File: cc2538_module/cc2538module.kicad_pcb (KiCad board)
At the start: 2 copper layers, 49 parts, among them CON1 USB-MICRO-B, J2 XBEE, P1 CONN_2, SW1 JS102011SCQN, U1 TPS769XX, U2 TPS6217X, U3 CC2538, X1 32MHZ, X2 32.768KHz, j9 JTAG

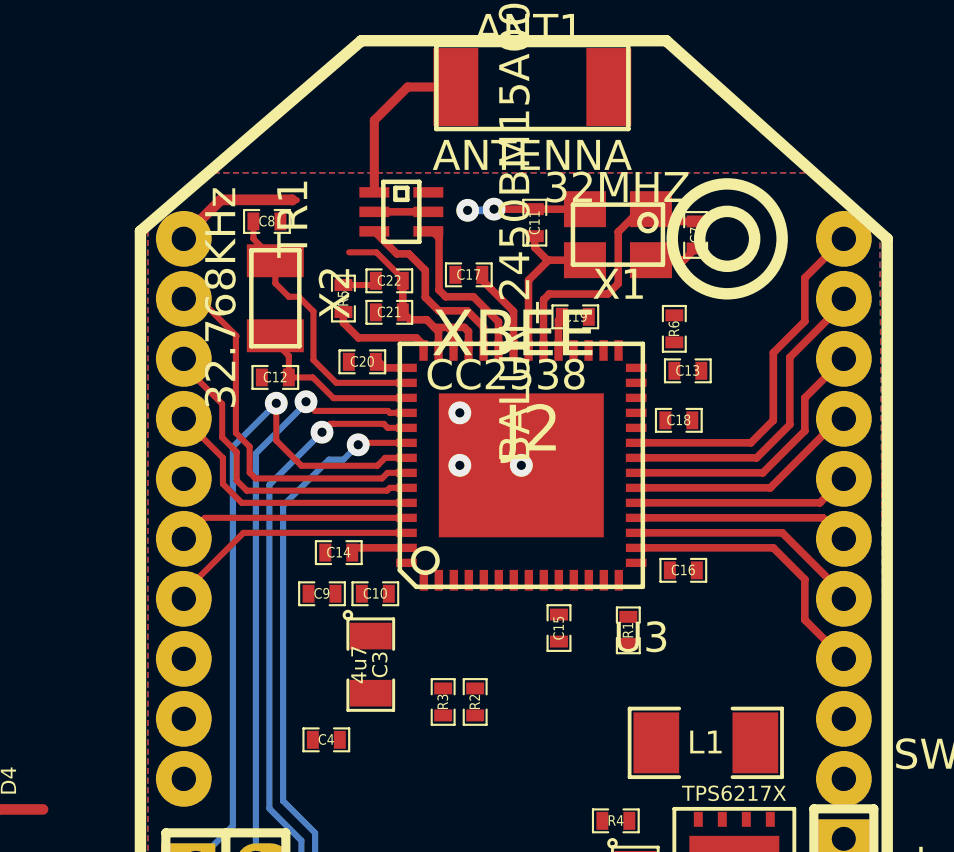
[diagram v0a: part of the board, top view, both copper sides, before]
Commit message: fixed some more routing to the pcb
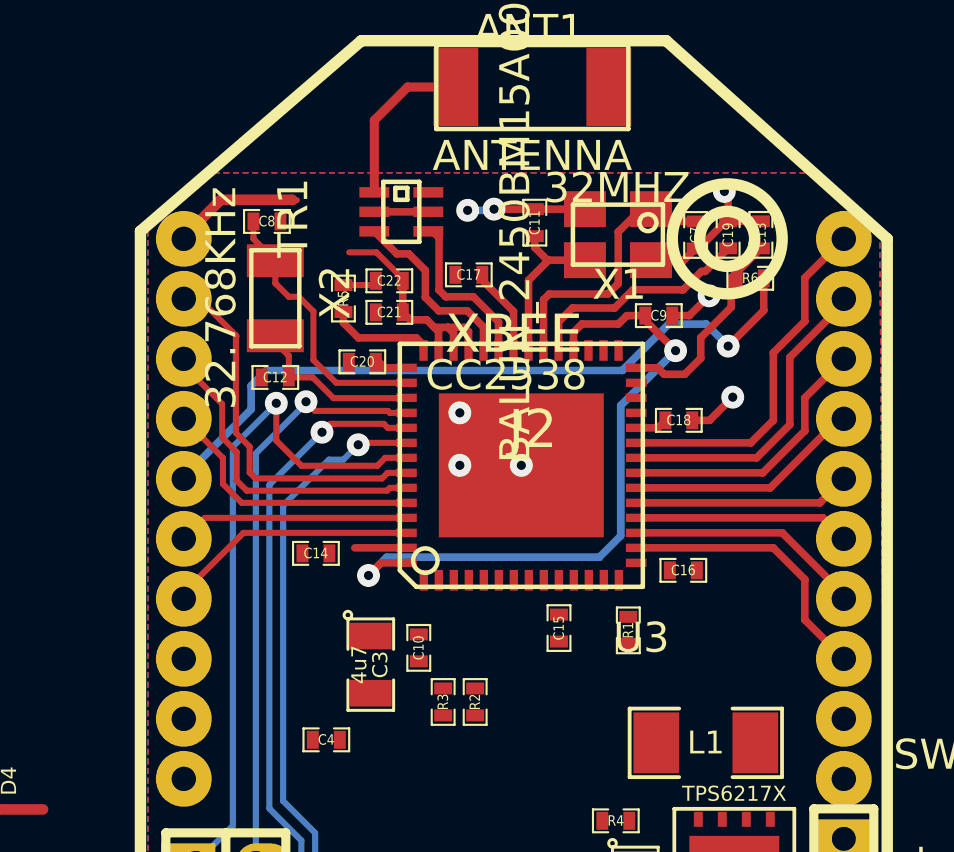
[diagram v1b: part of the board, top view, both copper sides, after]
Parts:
- moved C9 14.6 mm to (59.2, 32.4), turned to 0 degrees
- moved C19 5.78 mm to (61.5, 29.7), turned to 90 degrees
- moved C13 5.15 mm to (62.6, 29.7), turned to 90 degrees
- moved R6 3.04 mm to (62.3, 31.1), turned to 0 degrees
- moved C10 2.31 mm to (51.2, 43.4), turned to 270 degrees
- moved C14 0.76 mm to (47.8, 40.3)
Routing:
- net NRST: track 0.00 -> 23.8 mm, vias 0 -> 1
- net N-0000038: track 0.00 -> 22.1 mm, vias 0 -> 2
- net VDD: track 19.4 -> 26.9 mm
- net N-0000037: track 0.00 -> 7.33 mm
- net GND: track 31.2 -> 38.0 mm, vias 5 -> 8

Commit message: Finished top half of the PCB
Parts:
- moved C18 1.44 mm to (61.3, 35.9)
- moved R6 1.08 mm to (63.2, 31.6), turned to 270 degrees
- moved X2 0.42 mm to (46.1, 31.6)
- moved C8 0.40 mm to (45.8, 29.1), turned to 180 degrees
- moved R5 0.27 mm to (48.8, 31.5)
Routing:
- net VDD: track 26.9 -> 77.1 mm, vias 0 -> 6
- net GND: track 38.0 -> 61.9 mm, vias 8 -> 30
- net NRST: track 23.8 -> 23.2 mm
- net N-0000037: track 7.33 -> 7.91 mm
- net PB5: track 12.4 -> 12.1 mm, vias 0 -> 1

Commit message: Finisched layouting board
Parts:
- moved C5 19.6 mm to (46.4, 40.2)
- moved R9 18.6 mm to (53.7, 47.2), turned to 90 degrees
- moved R10 17.8 mm to (54.0, 45.5), turned to 180 degrees
- moved U1 17.4 mm to (49.2, 50.2), turned to 270 degrees
- moved R8 16.3 mm to (50.4, 44.9), turned to 180 degrees
- moved D2 15.9 mm to (49.9, 47.0)
- moved D3 15.9 mm to (51.2, 47.0)
- moved D4 15.9 mm to (52.5, 47.0)
- moved D1 15.9 mm to (48.5, 47.0)
- moved C2 15.6 mm to (45.8, 48.5), turned to 180 degrees
- moved R7 14.5 mm to (47.4, 45.1)
- moved SW1 12.5 mm to (61.9, 54.1), turned to 270 degrees
- moved R1 9.50 mm to (54.5, 51.6), turned to 180 degrees
- moved C4 6.90 mm to (45.4, 40.2), turned to 90 degrees
- moved R2 5.91 mm to (51.7, 51.0)
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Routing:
- net GND: track 61.9 -> 128.0 mm, vias 30 -> 37
- net VDD: track 77.1 -> 136.0 mm, vias 6 -> 10
- net VDD_USB: track 0.00 -> 26.1 mm, vias 0 -> 4
- net VDD_BCK: track 0.00 -> 21.5 mm
- net USB_N: track 0.00 -> 21.4 mm, vias 0 -> 2
- net NRST: track 23.2 -> 43.5 mm, vias 1 -> 2
- net PC0: track 0.00 -> 17.5 mm, vias 0 -> 2
- net USB_P: track 0.00 -> 17.2 mm, vias 0 -> 2
- net PC7: track 0.00 -> 14.0 mm
- net PC2: track 0.00 -> 13.7 mm
- net PB0: track 0.00 -> 12.6 mm
- net PC1: track 0.00 -> 11.6 mm
- net PC6: track 0.00 -> 9.81 mm
- net VIN: track 0.00 -> 9.34 mm
- net PC4: track 0.00 -> 8.40 mm
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
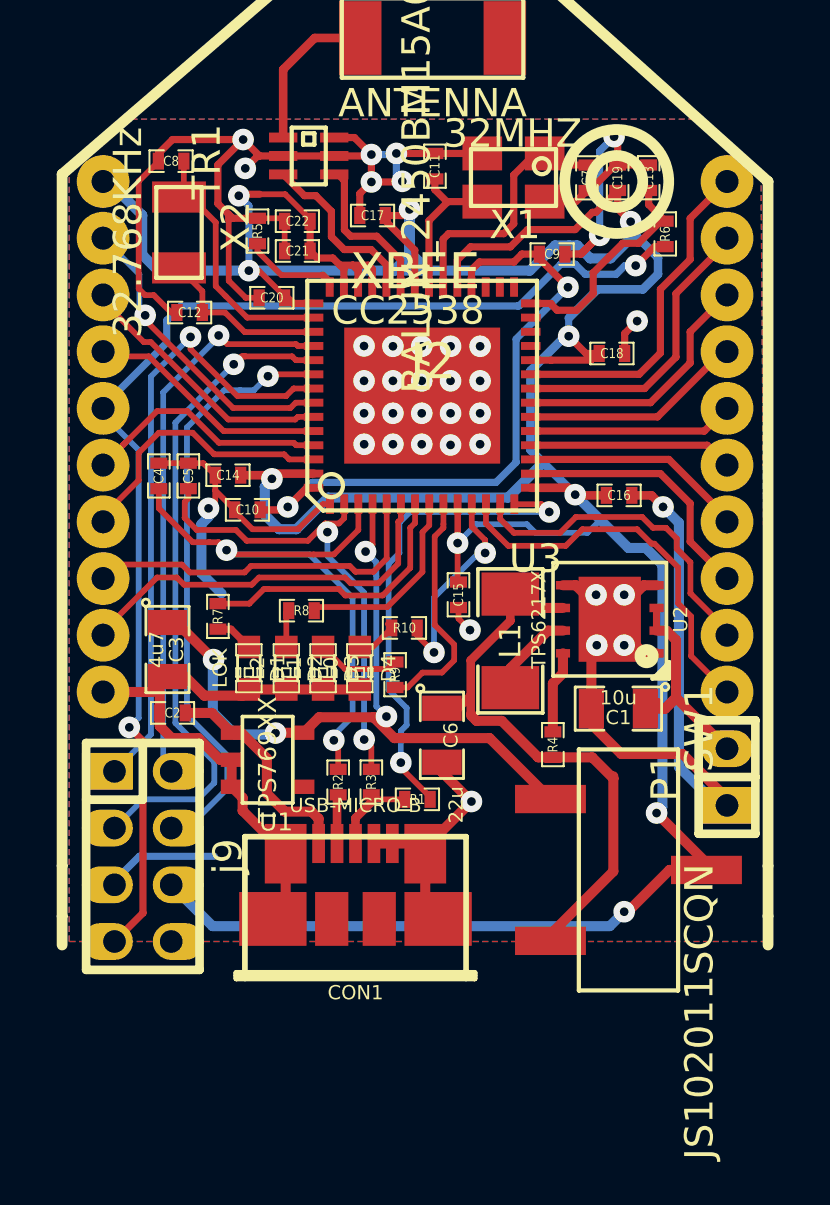
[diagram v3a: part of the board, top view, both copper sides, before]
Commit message: Moved usb connector to pcb edge
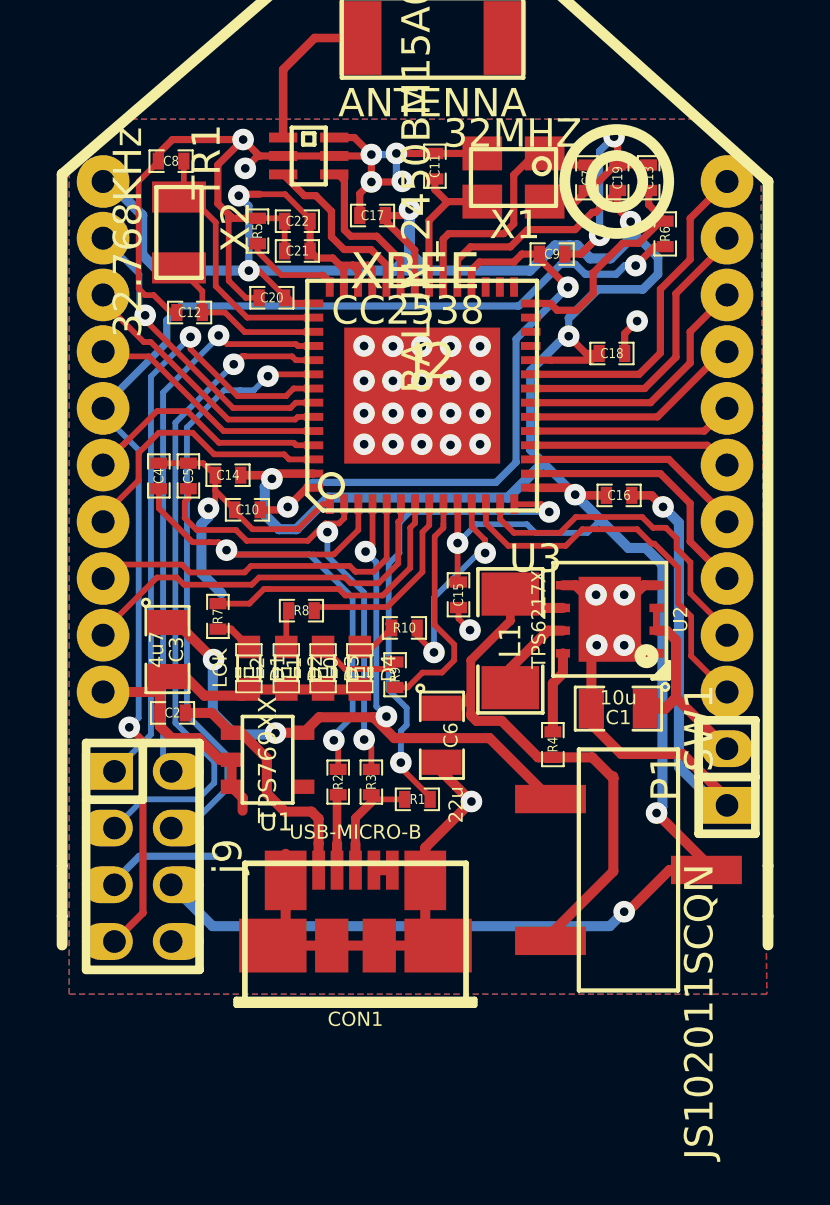
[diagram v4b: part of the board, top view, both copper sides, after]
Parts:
- moved CON1 0.94 mm to (52.3, 56.7)
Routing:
- net GND: track 128.0 -> 134.1 mm
- net N-0000012: track 1.73 -> 2.68 mm
- net VUSB_BUS: track 7.85 -> 8.79 mm
- net N-000004: track 3.19 -> 4.13 mm
